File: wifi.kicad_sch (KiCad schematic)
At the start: 9 parts, among them J3 WIFI_OFF

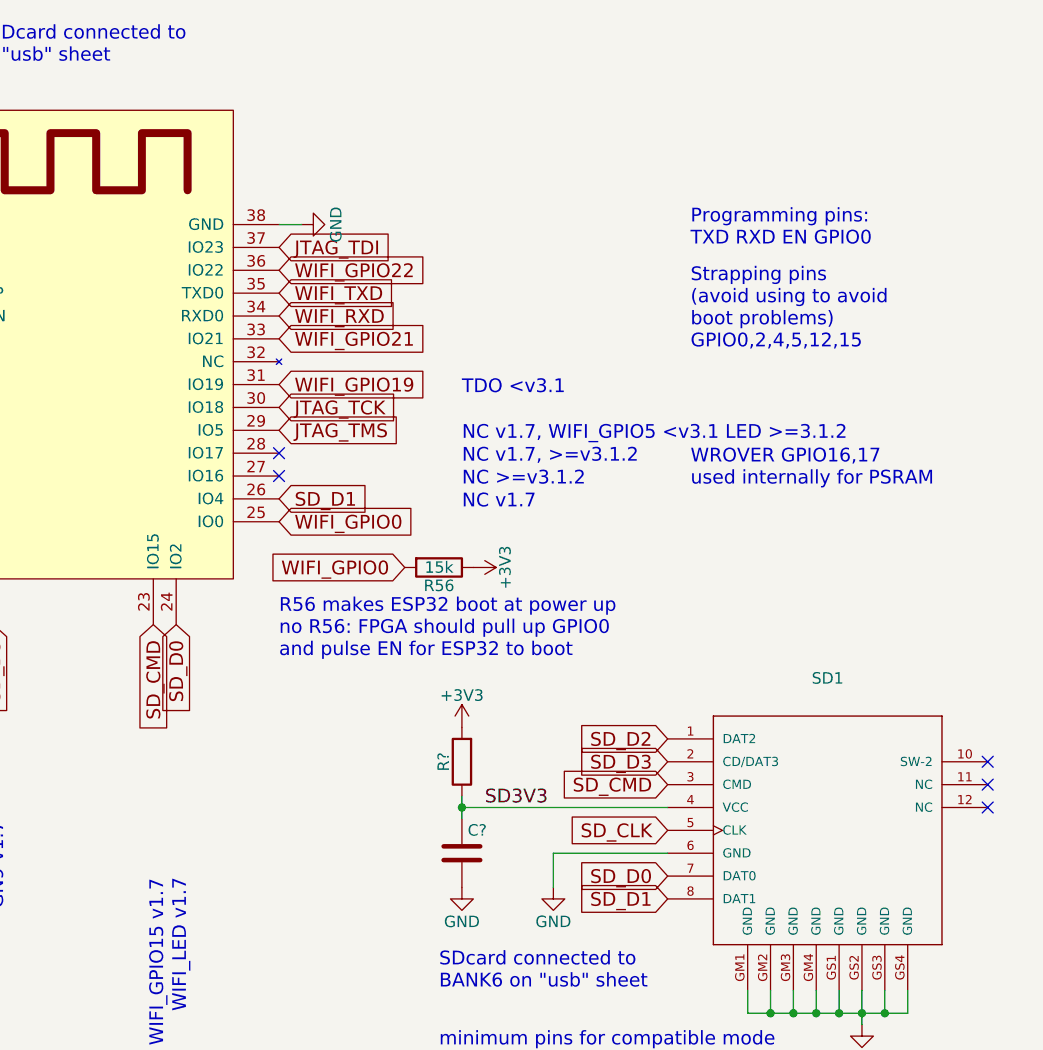
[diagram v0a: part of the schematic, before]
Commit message: Adding USB-C
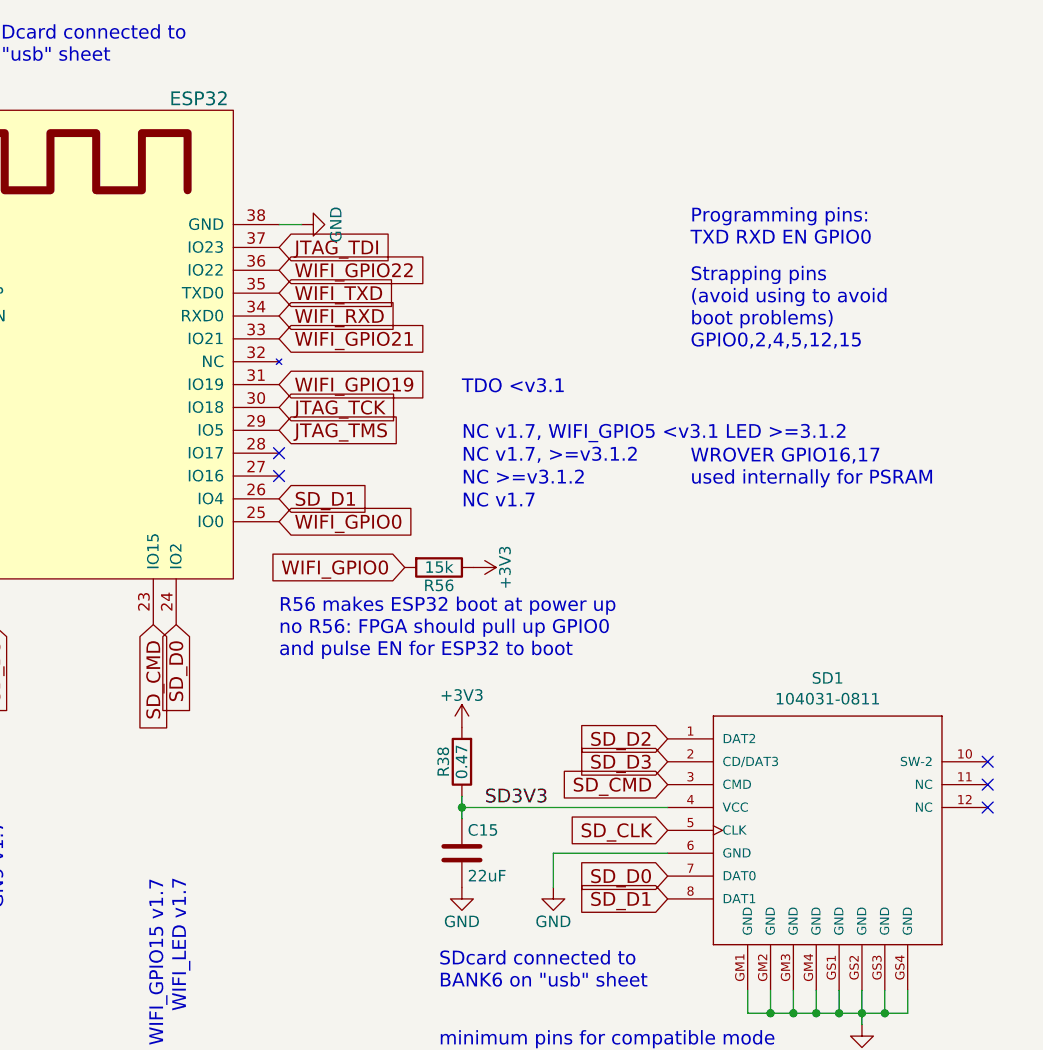
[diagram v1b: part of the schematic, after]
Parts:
- C15: renamed from C?; value (none) -> 22uF; footprint (none) -> Capacitor_SMD:C_0805_2012Metric
- R38: renamed from R?; value (none) -> 0.47; footprint (none) -> Resistor_SMD:R_0603_1608Metric
- SD1: value (none) -> 104031-0811; footprint (none) -> micro-sd-schd3a0100-104031-811:SCHD3A100-104031-0811
- U9: value (none) -> ESP32; footprint (none) -> ESP32:ESP32
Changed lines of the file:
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@@
   (title_block
     (title "ULX3S")
-    (rev "1.0.9")
+    (date "2023-01-19")
+    (rev "3.1.8")
     (company "EMARD")
     (comment 1 "WIFI module ESP32")
@@
       (effects (font (size 1.524 1.524)))
     )
-    (property "Value" "" (id 1) (at 182.88 55.88 0)
+    (property "Value" "ESP32" (id 1) (at 182.88 55.88 0)
       (effects (font (size 1.524 1.524)))
     )
-    (property "Footprint" "" (id 2) (at 177.8 53.34 0)
+    (property "Footprint" "ESP32:ESP32" (id 2) (at 177.8 53.34 0)
       (effects (font (size 1.524 1.524)) hide)
     )
@@
   (symbol (lib_id "Device:R") (at 212.09 129.54 180) (unit 1)
     (in_bom yes) (on_board yes)
-    (property "Reference" "R?" (id 0) (at 210.058 129.54 90))
-    (property "Value" "" (id 1) (at 212.09 129.54 90))
-    (property "Footprint" "" (id 2) (at 213.868 129.54 90)
+    (property "Reference" "R38" (id 0) (at 210.058 129.54 90))
+    (property "Value" "0.47" (id 1) (at 212.09 129.54 90))
+    (property "Footprint" "Resistor_SMD:R_0603_1608Metric" (id 2) (at 213.868 129.54 90)
       (effects (font (size 1.27 1.27)) hide)
     )
@@
   (symbol (lib_id "Device:C") (at 212.09 139.7 0) (unit 1)
     (in_bom yes) (on_board yes)
-    (property "Reference" "C?" (id 0) (at 212.725 137.16 0)
+    (property "Reference" "C15" (id 0) (at 212.725 137.16 0)
       (effects (font (size 1.27 1.27)) (justify left))
     )
-    (property "Value" "" (id 1) (at 212.725 142.24 0)
+    (property "Value" "22uF" (id 1) (at 212.725 142.24 0)
       (effects (font (size 1.27 1.27)) (justify left))
     )
-    (property "Footprint" "" (id 2) (at 213.0552 143.51 0)
+    (property "Footprint" "Capacitor_SMD:C_0805_2012Metric" (id 2) (at 213.0552 143.51 0)
       (effects (font (size 1.27 1.27)) hide)
     )
@@
     (in_bom yes) (on_board yes)
     (property "Reference" "SD1" (id 0) (at 252.73 120.269 0))
-    (property "Value" "" (id 1) (at 252.73 122.5804 0))
-    (property "Footprint" "" (id 2) (at 252.73 137.16 0)
+    (property "Value" "104031-0811" (id 1) (at 252.73 122.5804 0))
+    (property "Footprint" "micro-sd-schd3a0100-104031-811:SCHD3A100-104031-0811" (id 2) (at 252.73 137.16 0)
       (effects (font (size 1.27 1.27)) (justify left bottom) hide)
     )
